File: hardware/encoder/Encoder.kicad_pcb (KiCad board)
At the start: 2 copper layers, 14 x 18 mm, 3 parts, among them J7 ENCODER_8P, U27 MA735GGU-P

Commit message: Prepare self-assembled bench panel and order-readiness plan
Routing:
- added copper zone on In1.Cu, net GND
- added copper zone on In2.Cu, net GND
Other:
- copper layers 2 -> 4
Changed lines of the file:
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@@
 	(generator_version "10.0")
 	(general
-		(thickness 1.6)
+		(thickness 1.578)
 		(legacy_teardrops no)
 	)
@@
 	(layers
 		(0 "F.Cu" signal)
+		(4 "In1.Cu" signal)
+		(6 "In2.Cu" signal)
 		(2 "B.Cu" signal)
 		(9 "F.Adhes" user "F.Adhesive")
@@
 	)
 	(setup
+		(stackup
+			(layer "F.SilkS"
+				(type "Top Silk Screen")
+			)
+			(layer "F.Paste"
+				(type "Top Solder Paste")
+			)
+			(layer "F.Mask"
+				(type "Top Solder Mask")
+				(thickness 0.01)
+			)
+			(layer "F.Cu"
+				(type "copper")
+				(thickness 0.035)
+			)
+			(layer "dielectric 1"
+				(type "prepreg")
+				(thickness 0.109)
+				(material "2116 RC54%")
+				(epsilon_r 4.5)
+				(loss_tangent 0.02)
+			)
+			(layer "In1.Cu"
+				(type "copper")
+				(thickness 0.03)
+			)
+			(layer "dielectric 2"
+				(type "core")
+				(thickness 1.23)
+				(material "FR4 core 1.3mm 1/1oz with copper")
+				(epsilon_r 4.5)
+				(loss_tangent 0.02)
+			)
+			(layer "In2.Cu"
+				(type "copper")
+				(thickness 0.03)
+			)
+			(layer "dielectric 3"
+				(type "prepreg")
+				(thickness 0.109)
+				(material "2116 RC54%")
+				(epsilon_r 4.5)
+				(loss_tangent 0.02)
+			)
+			(layer "B.Cu"
+				(type "copper")
+				(thickness 0.035)
+			)
+			(layer "B.Mask"
+				(type "Bottom Solder Mask")
+				(thickness 0.01)
+			)
+			(layer "B.Paste"
+				(type "Bottom Solder Paste")
+			)
+			(layer "B.SilkS"
+				(type "Bottom Silk Screen")
+			)
+			(copper_finish "ENIG")
+			(dielectric_constraints yes)
+		)
 		(pad_to_mask_clearance 0)
 		(allow_soldermask_bridges_in_footprints no)
@@
 		(hatch edge 0.5)
 		(connect_pads
+			(clearance 0.15)
+		)
+		(min_thickness 0.15)
+		(fill yes
+			(thermal_gap 0.2)
+			(thermal_bridge_width 0.2)
+			(island_removal_mode 0)
+		)
+		(polygon
+			(pts
+				(xy 51.5 50.5) (xy 62.5 50.5) (xy 62.5 67.5) (xy 51.5 67.5)
+			)
+		)
+	)
+	(zone
+		(net "GND")
+		(layer "In1.Cu")
+		(name "ENCODER GND In1.Cu")
+		(hatch edge 0.5)
+		(connect_pads
+			(clearance 0.15)
+		)
+		(min_thickness 0.15)
+		(fill yes
+			(thermal_gap 0.2)
+			(thermal_bridge_width 0.2)
+			(island_removal_mode 0)
+		)
+		(polygon
+			(pts
+				(xy 51.5 50.5) (xy 62.5 50.5) (xy 62.5 67.5) (xy 51.5 67.5)
+			)
+		)
+	)
+	(zone
+		(net "GND")
+		(layer "In2.Cu")
+		(name "ENCODER GND In2.Cu")
+		(hatch edge 0.5)
+		(connect_pads

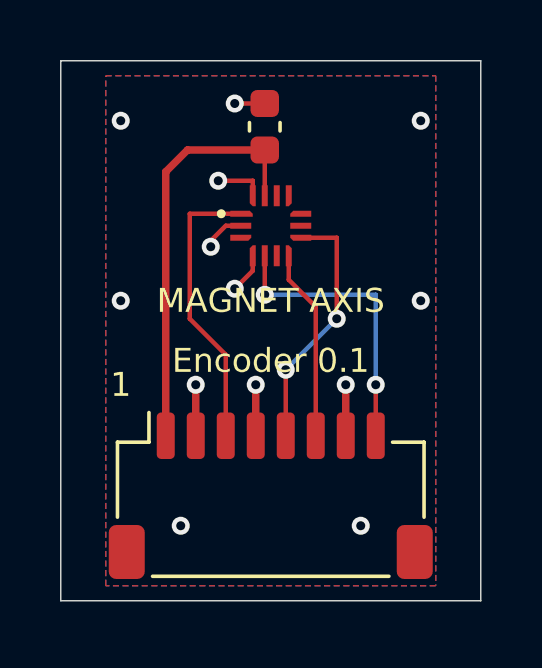
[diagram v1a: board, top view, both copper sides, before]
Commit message: Prepare wired Rev-A bench boards and submit manufacturing review
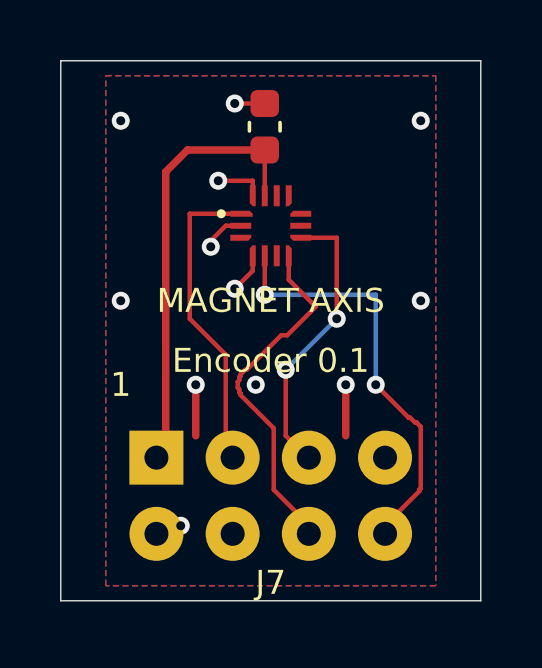
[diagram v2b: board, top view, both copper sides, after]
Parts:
- J7: value ENCODER_8P -> Soldered wires Signal_2x04; footprint Connector_JST:JST_SH_SM08B-SRSS-TB_1x08-1MP_P1.00mm_Horizontal -> MagMouseModular:Wire_Signal_2x04_P2.54mm
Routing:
- net ENC_CS_LOCAL: track 6.37 -> 11.8 mm
- net ENC_MISO_LOCAL: track 9.70 -> 14.1 mm
- net GND: track 10.5 -> 8.81 mm, vias 13 -> 12
- net ENC_MOSI_LOCAL: track 8.50 -> 9.59 mm

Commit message: Repair copper contacts and make manufacturing panel router-compatible
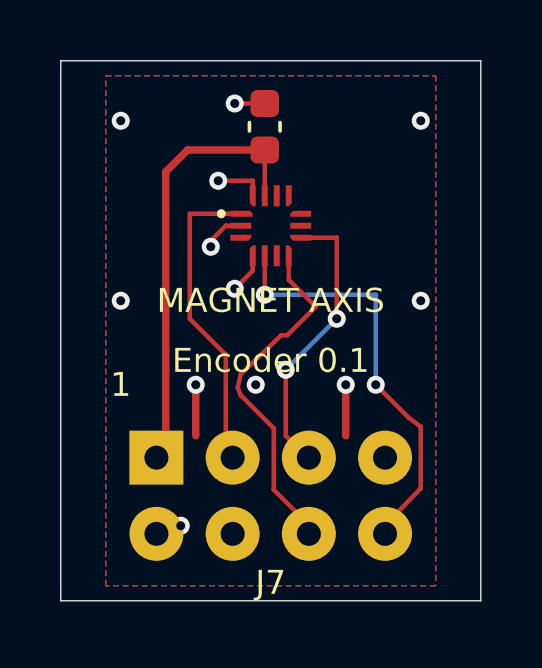
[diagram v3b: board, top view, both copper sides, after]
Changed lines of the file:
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@@
-	)
-	(segment
-		(start 61.65 61.9)
-		(end 61.8 62.05)
-		(width 0.15)
-		(layer "F.Cu")
-		(net "ENC_MISO_LOCAL")
-	)
-	(segment
-		(start 61.95 64.349999)
-		(end 60.9 65.4)
-		(width 0.15)
-		(layer "F.Cu")
-		(net "ENC_MISO_LOCAL")
 	)
 	(segment
 		(start 56.8 56.5)
 		(end 56.8 57.8)
-		(width 0.15)
-		(layer "F.Cu")
-		(net "ENC_MISO_LOCAL")
-	)
-	(segment
-		(start 61.6 61.9)
-		(end 61.65 61.9)
 		(width 0.15)
 		(layer "F.Cu")
@@
 	)
 	(segment
-		(start 61.95 64.3)
-		(end 61.95 64.349999)
-		(width 0.15)
-		(layer "F.Cu")
-		(net "ENC_MISO_LOCAL")
-	)
-	(segment
-		(start 61.85 62.05)
-		(end 62 62.2)
+		(start 60.9 65.4)
+		(end 62 64.25)
 		(width 0.15)
 		(layer "F.Cu")
@@
 	)
 	(segment
-		(start 62 64.25)
-		(end 61.95 64.3)
+		(start 62 62.2)
+		(end 61.6 61.9)
 		(width 0.15)
 		(layer "F.Cu")
@@
 		(start 60.5 60.8)
 		(end 61.6 61.9)
-		(width 0.15)
-		(layer "F.Cu")
-		(net "ENC_MISO_LOCAL")
-	)
-	(segment
-		(start 61.8 62.05)
-		(end 61.85 62.05)
 		(width 0.15)
 		(layer "F.Cu")
@@
 	)
 	(segment
-		(start 55.95 60.55)
-		(end 55.95 60.65)
+		(start 56 61.15)
+		(end 55.9 60.9)
 		(width 0.15)
 		(layer "F.Cu")
@@
 	)
 	(segment
-		(start 56.2 60.3)
-		(end 56.15 60.3)
-		(width 0.15)
-		(layer "F.Cu")
-		(net "ENC_CS_LOCAL")
-	)
-	(segment
-		(start 57.35 59.15)
-		(end 56.2 60.3)
+		(start 55.9 60.9)
+		(end 56 60.45)
 		(width 0.15)
 		(layer "F.Cu")
@@
 	)
 	(segment
-		(start 56 60.45)
-		(end 56 60.5)
-		(width 0.15)
-		(layer "F.Cu")
-		(net "ENC_CS_LOCAL")
-	)
-	(segment
 		(start 58.15 65.5)
 		(end 58.2 65.55)
-		(width 0.15)
-		(layer "F.Cu")
-		(net "ENC_CS_LOCAL")
-	)
-	(segment
-		(start 55.9 60.7)
-		(end 55.9 60.9)
 		(width 0.15)
 		(layer "F.Cu")
@@
 	)
 	(segment
-		(start 55.9 60.9)
-		(end 55.95 60.95)
-		(width 0.15)
-		(layer "F.Cu")
-		(net "ENC_CS_LOCAL")
-	)
-	(segment
-		(start 55.95 61.05)
-		(end 56 61.1)
-		(width 0.15)
-		(layer "F.Cu")
-		(net "ENC_CS_LOCAL")
-	)
-	(segment
 		(start 57.1 64.3)
 		(end 58.15 65.349999)
-		(width 0.15)
-		(layer "F.Cu")
-		(net "ENC_CS_LOCAL")
-	)
-	(segment
-		(start 55.95 60.95)
-		(end 55.95 61.05)
-		(width 0.15)
-		(layer "F.Cu")
-		(net "ENC_CS_LOCAL")
-	)
-	(segment
-		(start 56.15 60.3)
-		(end 56 60.45)
-		(width 0.15)
-		(layer "F.Cu")
-		(net "ENC_CS_LOCAL")
-	)
-	(segment
-		(start 56 61.1)
-		(end 56 61.15)
 		(width 0.15)
 		(layer "F.Cu")
@@
 	)
 	(segment
-		(start 55.95 60.65)
-		(end 55.9 60.7)
-		(width 0.15)
-		(layer "F.Cu")
-		(net "ENC_CS_LOCAL")
-	)
-	(segment
 		(start 58.2 65.65)
 		(end 58.25 65.7)
@@
 	)
 	(segment
-		(start 56 60.5)
-		(end 55.95 60.55)
+		(start 56 60.45)
+		(end 57.35 59.15)
 		(width 0.15)
 		(layer "F.Cu")
